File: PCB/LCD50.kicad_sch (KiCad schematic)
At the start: 33 parts, among them J701 FFC2B28-40-G, J702 Conn_01x06_Female, SW701 SW_PUSH, SW702 SW_PUSH, SW703 SW_PUSH, SW704 SW_PUSH, U20 xc7z020clg484, U701 MT3608

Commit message: [+] routing done, need to fix minor errors.
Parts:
- gave numbers to parts that had none: 4
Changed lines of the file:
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@@
 	)
 	(label "LCDGREEN4"
-		(at 156.21 80.01 0)
+		(at 163.83 80.01 0)
 		(fields_autoplaced yes)
 		(effects
@@
 	)
 	(label "LCDGREEN6"
-		(at 157.48 85.09 0)
+		(at 163.195 85.09 0)
 		(fields_autoplaced yes)
 		(effects
@@
 		(on_board yes)
 		(dnp no)
-		(property "Reference" "Q?"
+		(property "Reference" "Q8"
 			(at 36.195 193.6496 0)
 			(effects
@@
 		(instances
 			(project "DFTBoard"
-				(path "/0cf42e13-7c72-4f5f-898b-a3f851b94890/00000000-0000-0000-0000-000058508444"
-					(reference "Q?")
-					(unit 1)
-				)
-				(path "/0cf42e13-7c72-4f5f-898b-a3f851b94890/00000000-0000-0000-0000-00005852a88e"
-					(reference "Q?")
-					(unit 1)
-				)
 				(path "/0cf42e13-7c72-4f5f-898b-a3f851b94890/00000000-0000-0000-0000-00005c7c62ae"
 					(reference "Q8")
@@
 		(on_board yes)
 		(dnp no)
-		(property "Reference" "#PWR?"
+		(property "Reference" "#PWR0169"
 			(at 38.735 202.565 0)
 			(effects
@@
 		(instances
 			(project "DFTBoard"
-				(path "/0cf42e13-7c72-4f5f-898b-a3f851b94890/00000000-0000-0000-0000-000058508444"
-					(reference "#PWR?")
-					(unit 1)
-				)
-				(path "/0cf42e13-7c72-4f5f-898b-a3f851b94890/00000000-0000-0000-0000-00005852a88e"
-					(reference "#PWR?")
-					(unit 1)
-				)
 				(path "/0cf42e13-7c72-4f5f-898b-a3f851b94890/00000000-0000-0000-0000-00005c7c62ae"
 					(reference "#PWR0169")
@@
 		(on_board yes)
 		(dnp no)
-		(property "Reference" "R?"
+		(property "Reference" "R77"
 			(at 27.813 191.897 0)
 			(effects
@@
 		(instances
 			(project "DFTBoard"
-				(path "/0cf42e13-7c72-4f5f-898b-a3f851b94890/00000000-0000-0000-0000-000058508444"
-					(reference "R?")
-					(unit 1)
-				)
-				(path "/0cf42e13-7c72-4f5f-898b-a3f851b94890/00000000-0000-0000-0000-00005852a88e"
-					(reference "R?")
-					(unit 1)
-				)
 				(path "/0cf42e13-7c72-4f5f-898b-a3f851b94890/00000000-0000-0000-0000-00005c7c62ae"
 					(reference "R77")
@@
 		(on_board yes)
 		(dnp no)
-		(property "Reference" "D?"
+		(property "Reference" "D4"
 			(at 36.195 177.165 0)
 			(effects
@@
 		(instances
 			(project "DFTBoard"
-				(path "/0cf42e13-7c72-4f5f-898b-a3f851b94890/00000000-0000-0000-0000-000058508444"
-					(reference "D?")
-					(unit 1)
-				)
-				(path "/0cf42e13-7c72-4f5f-898b-a3f851b94890/00000000-0000-0000-0000-00005852a88e"
-					(reference "D?")
-					(unit 1)
-				)
 				(path "/0cf42e13-7c72-4f5f-898b-a3f851b94890/00000000-0000-0000-0000-00005c7c62ae"
 					(reference "D4")
@@
 		(on_board yes)
 		(dnp no)
-		(property "Reference" "R?"
+		(property "Reference" "R78"
 			(at 37.973 166.497 0)
 			(effects
@@
 		(instances
 			(project "DFTBoard"
-				(path "/0cf42e13-7c72-4f5f-898b-a3f851b94890/00000000-0000-0000-0000-000058508444"
-					(reference "R?")
-					(unit 1)
-				)
-				(path "/0cf42e13-7c72-4f5f-898b-a3f851b94890/00000000-0000-0000-0000-00005852a88e"
-					(reference "R?")
-					(unit 1)
-				)
 				(path "/0cf42e13-7c72-4f5f-898b-a3f851b94890/00000000-0000-0000-0000-00005c7c62ae"
 					(reference "R78")
@@
 		(on_board yes)
 		(dnp no)
-		(property "Reference" "#PWR?"
+		(property "Reference" "#PWR0168"
 			(at 38.735 167.005 0)
 			(effects
@@
 		(instances
 			(project "DFTBoard"
-				(path "/0cf42e13-7c72-4f5f-898b-a3f851b94890/00000000-0000-0000-0000-000058508444"
-					(reference "#PWR?")
-					(unit 1)
-				)
-				(path "/0cf42e13-7c72-4f5f-898b-a3f851b94890/00000000-0000-0000-0000-00005852a88e"
-					(reference "#PWR?")
-					(unit 1)
-				)
 				(path "/0cf42e13-7c72-4f5f-898b-a3f851b94890/00000000-0000-0000-0000-00005c7c62ae"
 					(reference "#PWR0168")

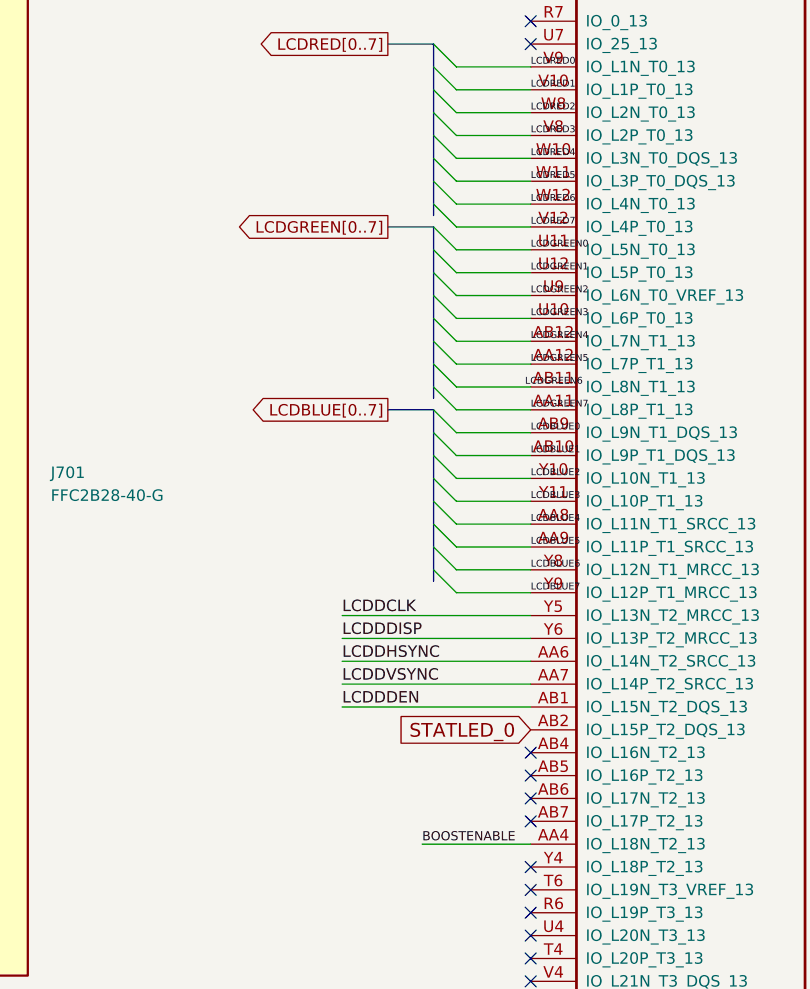
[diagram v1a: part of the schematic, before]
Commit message: Resolved most of the errors
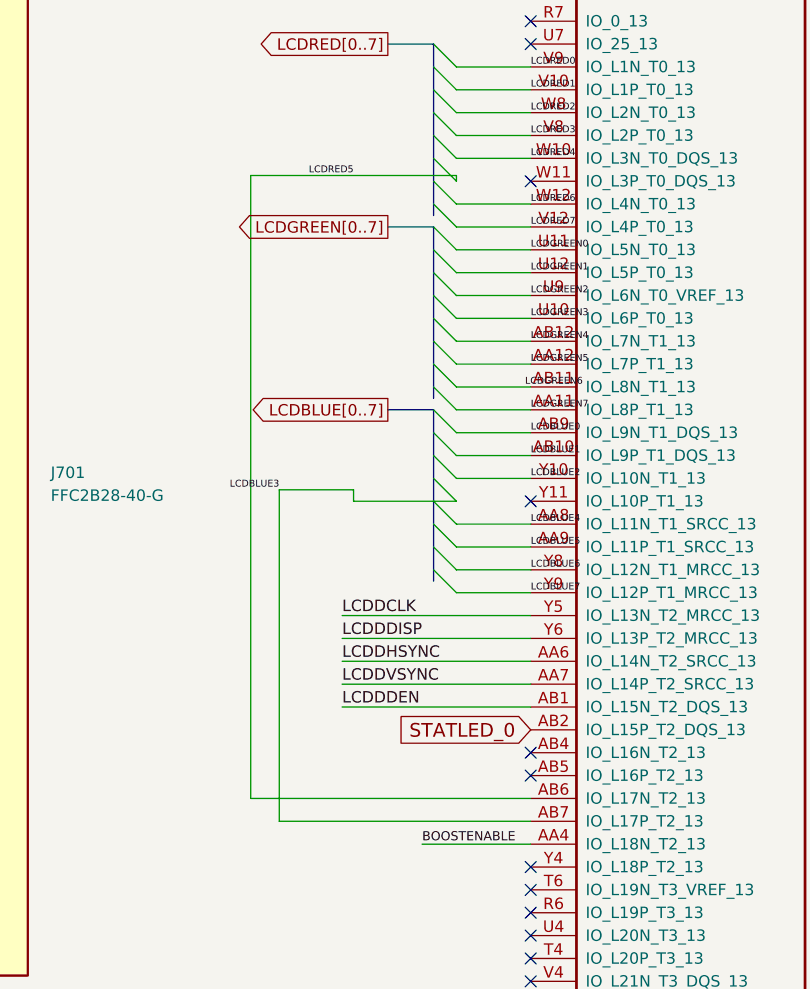
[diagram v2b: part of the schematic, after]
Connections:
- net LCDBLUE3: now also U20.AB7 (IO_L17P_T2_13); no longer U20.Y11 (IO_L10P_T1_13)
- net LCDRED5: now also U20.AB6 (IO_L17N_T2_13); no longer U20.W11 (IO_L3P_T0_DQS_13)
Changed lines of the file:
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@@
+	)
+	(no_connect
+		(at 163.83 62.23)
 	)
 	(no_connect
@@
 	)
 	(no_connect
-		(at 163.83 130.81)
-	)
-	(no_connect
 		(at 92.71 130.175)
 	)
@@
 	)
 	(no_connect
+		(at 163.83 97.79)
+	)
+	(no_connect
 		(at 92.71 135.255)
 	)
@@
 	)
 	(no_connect
-		(at 163.83 133.35)
-	)
-	(no_connect
 		(at 163.83 151.13)
 	)
@@
 	(wire
 		(pts
+			(xy 132.715 61.595) (xy 132.715 130.81)
+		)
+		(stroke
+			(width 0)
+			(type default)
+		)
+	)
+	(wire
+		(pts
 			(xy 71.755 117.475) (xy 92.71 117.475)
 		)
@@
 	(wire
 		(pts
+			(xy 132.715 61.595) (xy 155.575 61.595)
+		)
+		(stroke
+			(width 0)
+			(type default)
+		)
+	)
+	(wire
+		(pts
 			(xy 73.025 174.625) (xy 85.09 174.625)
 		)
@@
 	(wire
 		(pts
-			(xy 155.575 97.79) (xy 163.83 97.79)
-		)
-		(stroke
-			(width 0)
-			(type default)
-		)
-	)
-	(wire
-		(pts
 			(xy 53.975 53.975) (xy 51.435 53.975)
 		)
@@
 		)
 	)
+	(wire
+		(pts
+			(xy 135.89 133.35) (xy 163.83 133.35)
+		)
+		(stroke
+			(width 0)
+			(type default)
+		)
+	)
 	(bus
 		(pts
@@
 		)
 	)
+	(wire
+		(pts
+			(xy 155.575 61.595) (xy 155.575 62.23)
+		)
+		(stroke
+			(width 0)
+			(type default)
+		)
+	)
 	(bus
 		(pts
@@
 		)
 	)
+	(wire
+		(pts
+			(xy 153.035 97.79) (xy 144.145 97.79)
+		)
+		(stroke
+			(width 0)
+			(type default)
+		)
+	)
 	(bus
 		(pts
@@
 	(wire
 		(pts
-			(xy 155.575 62.23) (xy 163.83 62.23)
+			(xy 135.89 96.52) (xy 135.89 133.35)
 		)
 		(stroke
@@
 	(wire
 		(pts
+			(xy 132.715 130.81) (xy 163.83 130.81)
+		)
+		(stroke
+			(width 0)
+			(type default)
+		)
+	)
+	(wire
+		(pts
 			(xy 155.575 85.09) (xy 163.83 85.09)
 		)
@@
 	(wire
 		(pts
+			(xy 144.145 96.52) (xy 135.89 96.52)
+		)
+		(stroke
+			(width 0)
+			(type default)
+		)
+	)
+	(wire
+		(pts
 			(xy 151.13 186.69) (xy 151.13 184.15)
 		)
@@
 	(wire
 		(pts
+			(xy 155.575 97.79) (xy 153.035 97.79)
+		)
+		(stroke
+			(width 0)
+			(type default)
+		)
+	)
+	(wire
+		(pts
 			(xy 157.48 186.69) (xy 163.83 186.69)
 		)
@@
 		(pts
 			(xy 73.025 172.085) (xy 85.09 172.085)
+		)
+		(stroke
+			(width 0)
+			(type default)
+		)
+	)
+	(wire
+		(pts
+			(xy 144.145 97.79) (xy 144.145 96.52)
 		)
 		(stroke
@@
 		)
 	)
+	(label "LCDBLUE3"
+		(at 135.89 96.52 180)
+		(fields_autoplaced yes)
+		(effects
+			(font
+				(size 0.762 0.762)
+			)
+			(justify right bottom)
+		)
+	)
 	(label "LCDRED7"
 		(at 92.71 71.755 0)
@@
 		)
 	)
-	(label "LCDRED5"
-		(at 163.83 62.23 0)
-		(fields_autoplaced yes)
-		(effects
-			(font
-				(size 0.762 0.762)
-			)
-			(justify left bottom)
-		)
-	)
 	(label "LCDRED3"
 		(at 92.71 61.595 0)
@@
 		)
 	)
-	(label "LCDBLUE3"
-		(at 163.83 97.79 0)
-		(fields_autoplaced yes)
-		(effects
-			(font
-				(size 0.762 0.762)
-			)
-			(justify left bottom)
-		)
-	)
 	(label "LCDRED1"
 		(at 92.71 56.515 0)
@@
 		)
 	)
+	(label "LCDRED5"
+		(at 144.145 61.595 180)
+		(fields_autoplaced yes)
+		(effects
+			(font
+				(size 0.762 0.762)
+			)
+			(justify right bottom)
+		)
+	)

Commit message: [+] complete PCB design
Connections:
- net +3V3: now also J702.1 (Pin_1); no longer J702.6 (Pin_6)
- net GND: now also J702.2 (Pin_2); no longer J702.5 (Pin_5)
- net JOYCS: now also J702.6 (Pin_6); no longer J702.1 (Pin_1)
- net JOYMISO: now also J702.4 (Pin_4); no longer J702.3 (Pin_3)
- net JOYMOSI: now also J702.5 (Pin_5); no longer J702.2 (Pin_2)
- net JOYSCK: now also J702.3 (Pin_3); no longer J702.4 (Pin_4)
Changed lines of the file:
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@@
 	)
 	(symbol
-		(lib_id "Connector:Conn_01x06_Female")
-		(at 90.17 172.085 0)
-		(unit 1)
-		(exclude_from_sim no)
-		(in_bom yes)
-		(on_board yes)
-		(dnp no)
-		(fields_autoplaced yes)
-		(property "Reference" "J702"
-			(at 91.44 172.0849 0)
-			(effects
-				(font
-					(size 1.27 1.27)
-				)
-				(justify left)
-			)
-		)
-		(property "Value" "Conn_01x06_Female"
-			(at 91.44 174.6249 0)
-			(effects
-				(font
-					(size 1.27 1.27)
-				)
-				(justify left)
-			)
-		)
-		(property "Footprint" "Connector_PinSocket_2.54mm:PinSocket_1x06_P2.54mm_Horizontal"
-			(at 90.17 172.085 0)
-			(effects
-				(font
-					(size 1.27 1.27)
-				)
-				(hide yes)
-			)
-		)
-		(property "Datasheet" "~"
-			(at 90.17 172.085 0)
-			(effects
-				(font
-					(size 1.27 1.27)
-				)
-				(hide yes)
-			)
-		)
-		(property "Description" "Generic connector, single row, 01x06, script generated (kicad-library-utils/schlib/autogen/connector/)"
-			(at 90.17 172.085 0)
-			(effects
-				(font
-					(size 1.27 1.27)
-				)
-				(hide yes)
-			)
-		)
-		(pin "4"
-		)
-		(pin "3"
-		)
-		(pin "6"
-		)
-		(pin "1"
-		)
-		(pin "2"
-		)
-		(pin "5"
-		)
-		(instances
-			(project "DFTBoard"
-				(path "/0cf42e13-7c72-4f5f-898b-a3f851b94890/00000000-0000-0000-0000-00005c7c62ae"
-					(reference "J702")
-					(unit 1)
-				)
-			)
-		)
-	)
-	(symbol
 		(lib_id "Device:R_Small")
 		(at 51.435 56.515 0)
@@
 					(unit 1)
 				)
+			)
+		)
+	)
+	(symbol
+		(lib_id "Connector:Conn_01x06_Female")
+		(at 90.17 174.625 0)
+		(mirror x)
+		(unit 1)
+		(exclude_from_sim no)
+		(in_bom yes)
+		(on_board yes)
+		(dnp no)
+		(property "Reference" "J702"
+			(at 91.44 174.6251 0)
+			(effects
+				(font
+					(size 1.27 1.27)
+				)
+				(justify left)
+			)
+		)
+		(property "Value" "Conn_01x06_Female"
+			(at 91.44 172.0851 0)
+			(effects
+				(font
+					(size 1.27 1.27)
+				)
+				(justify left)
+			)
+		)
+		(property "Footprint" "Connector_PinSocket_2.54mm:PinSocket_1x06_P2.54mm_Horizontal"
+			(at 90.17 174.625 0)
+			(effects
+				(font
+					(size 1.27 1.27)
+				)
+				(hide yes)
+			)
+		)
+		(property "Datasheet" "~"
+			(at 90.17 174.625 0)
+			(effects
+				(font
+					(size 1.27 1.27)
+				)
+				(hide yes)
+			)
+		)
+		(property "Description" "Generic connector, single row, 01x06, script generated (kicad-library-utils/schlib/autogen/connector/)"
+			(at 90.17 174.625 0)
+			(effects
+				(font
+					(size 1.27 1.27)
+				)
+				(hide yes)
+			)
+		)
+		(pin "4"
+		)
+		(pin "3"
+		)
+		(pin "6"
+		)
+		(pin "1"
+		)
+		(pin "2"
+		)
+		(pin "5"
+		)
+		(instances
+			(project "DFTBoard"
+				(path "/0cf42e13-7c72-4f5f-898b-a3f851b94890/00000000-0000-0000-0000-00005c7c62ae"
+					(reference "J702")
+					(unit 1)
+				)
